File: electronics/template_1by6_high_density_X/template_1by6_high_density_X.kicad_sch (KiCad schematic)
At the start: 8 parts, among them J1 1, J2 2, J3 3, J4 4, J5 5, J6 6

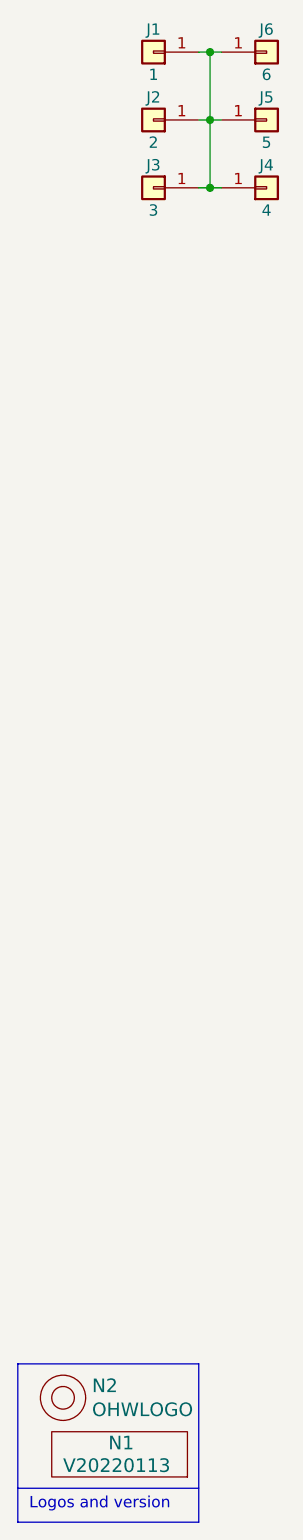
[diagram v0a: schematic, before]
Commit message: added Kosmos high density X templates and completed high density XN templates
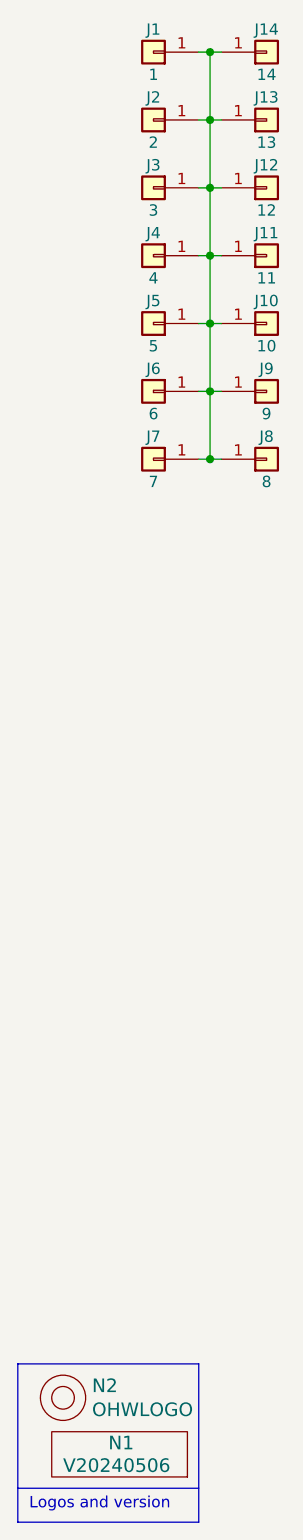
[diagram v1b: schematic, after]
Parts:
- added J10: 10, mill-max:PC_pin_nail_head_6092, symbol Connector_Generic:Conn_01x01
- added J11: 11, mill-max:PC_pin_nail_head_6092, symbol Connector_Generic:Conn_01x01
- added J12: 12, mill-max:PC_pin_nail_head_6092, symbol Connector_Generic:Conn_01x01
- added J13: 13, mill-max:PC_pin_nail_head_6092, symbol Connector_Generic:Conn_01x01
- added J14: 14, mill-max:PC_pin_nail_head_6092, symbol Connector_Generic:Conn_01x01
- added J7: 7, mill-max:PC_pin_nail_head_6092, symbol Connector_Generic:Conn_01x01
- added J8: 8, mill-max:PC_pin_nail_head_6092, symbol Connector_Generic:Conn_01x01
- added J9: 9, mill-max:PC_pin_nail_head_6092, symbol Connector_Generic:Conn_01x01
- N1: value V20220113 -> V20240506
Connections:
- net at J1.1 (Pin_1), J2.1 (Pin_1), J3.1 (Pin_1)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: now also J10.1 (Pin_1), J11.1 (Pin_1), J12.1 (Pin_1), J13.1 (Pin_1), J14.1 (Pin_1), J7.1 (Pin_1), J8.1 (Pin_1), J9.1 (Pin_1)
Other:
- moved on the sheet: J4, J5, J6
